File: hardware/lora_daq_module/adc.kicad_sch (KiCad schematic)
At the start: 0 parts

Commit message: added ADC input filter schematic
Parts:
- added C1: 47nF, symbol Device:C
- added C3: 0.1uF, symbol Device:C
- added D1, D2: D, symbol Device:D
- added J2: Conn_01x04, symbol Connector_Generic:Conn_01x04
- added R1: 1k, symbol Device:R
- added R3, R4: 10k, symbol Device:R
- added U1: ADS1115IDGS, Package_SO:TSSOP-10_3x3mm_P0.5mm, symbol Analog_ADC:ADS1115IDGS
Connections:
- new net: D1.2 (A), D2.2 (A), J2.1 (Pin_1), R1.2
- new net: C1.1, R1.1, U1.4 (AIN0)
- new net: J2.3 (Pin_3), U1.6 (AIN2)
- new net +3.3V: C3.1, D1.1 (K), R3.1, R4.1, U1.8 (VDD)
- new net GND: C1.2, C3.2, D2.1 (K), J2.2 (Pin_2), U1.1 (ADDR), U1.3 (GND), U1.5 (AIN1), U1.7 (AIN3)
- new net GPIO: U1.2 (ALERT/RDY)
- new net Input/5V: J2.4 (Pin_4)
- new net SCL: R3.2, U1.10 (SCL)
- new net SDA: R4.2, U1.9 (SDA)

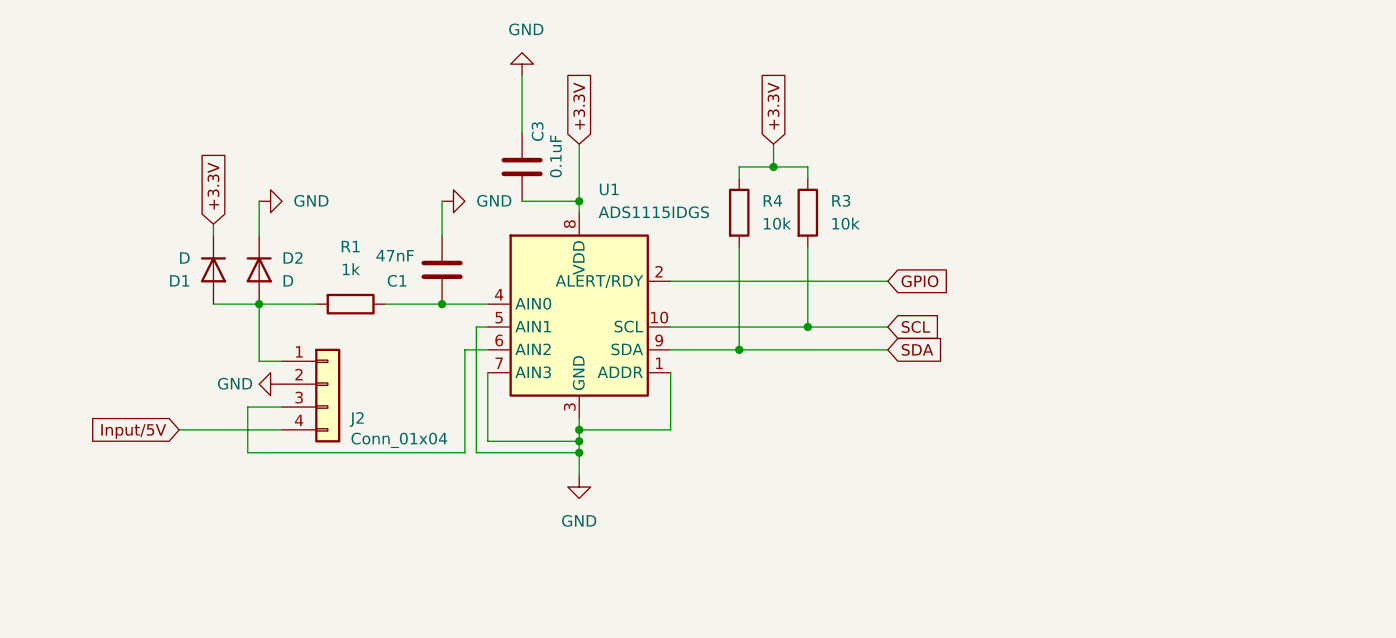
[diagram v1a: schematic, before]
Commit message: Updated the Adc circuit w/filters
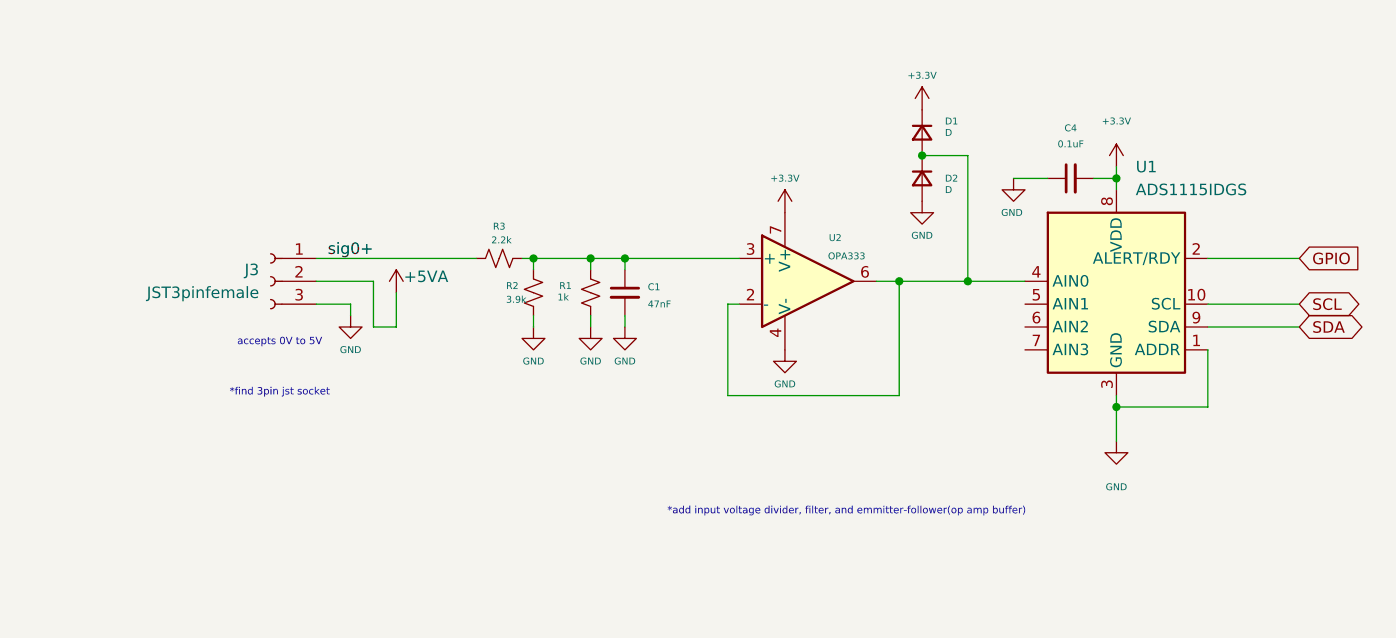
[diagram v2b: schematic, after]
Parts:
- removed C1: 47nF, symbol Device:C
- removed C3: 0.1uF, symbol Device:C
- removed D1, D2: D, symbol Device:D
- removed J2: Conn_01x04, symbol Connector_Generic:Conn_01x04
- removed R1: 1k, symbol Device:R
- removed R3, R4: 10k, symbol Device:R
- added C1: 47nF, symbol Device:C_Small
- added C4: 0.1uF, symbol Device:C_Small
- added D1, D2: D, symbol Device:D_Small
- added J3: JST3pinfemale, symbol Connector:Conn_01x03_Socket
- added R1: 1k, symbol Device:R_Small_US
- added R2: 3.9k, symbol Device:R_Small_US
- added R3: 2.2k, symbol Device:R_Small_US
- added U2: OPA333, Package_SO:SOIC-8_3.9x4.9mm_P1.27mm, symbol Amplifier_Operational:OPA333xxD
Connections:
- net +3.3V: now also C4.2, D1.1 (K), U2.7 (V+)
- net GND: now also C1.2, C4.1, D2.2 (A), J3.3 (Pin_3), R1.1, R2.2, U2.4 (V-); no longer U1.5 (AIN1), U1.7 (AIN3)
- net at U1.4 (AIN0): now also D1.2 (A), D2.1 (K), U2.2 (-), U2.6
- new net: C1.1, R1.2, R2.1, R3.2, U2.3 (+)
- new net +5VA: J3.2 (Pin_2)
- new net sig0+: J3.1 (Pin_1), R3.1
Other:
- note added: "*add input voltage divider, filter, and emmitter-follower(op amp buffer)"
- note added: "*find 3pin jst socket"
- note added: "accepts 0V to 5V"
- moved on the sheet: U1

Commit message: modified ADC input filter schematic
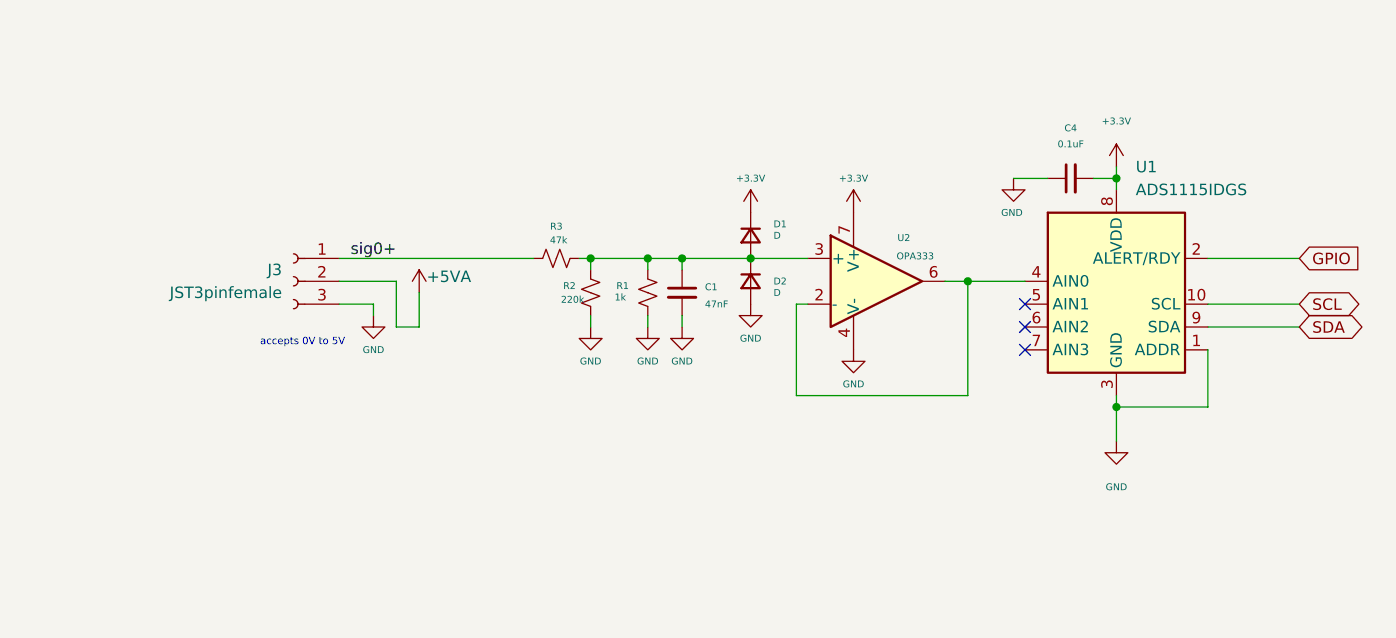
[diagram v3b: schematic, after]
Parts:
- R2: value 3.9k -> 220k
- R3: value 2.2k -> 47k
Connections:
- net at C1.1, R1.2, R2.1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: now also D1.2 (A), D2.1 (K)
- net at U1.4 (AIN0), U2.2 (-), U2.6: no longer D1.2 (A), D2.1 (K)
- no-connect marks 0 -> 3
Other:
- note removed: "*add input voltage divider, filter, and emmitter-follower(op amp buffer)"
- note removed: "*find 3pin jst socket"
- moved on the sheet: C1, D1, D2, J3, R1, R2, R3, U2

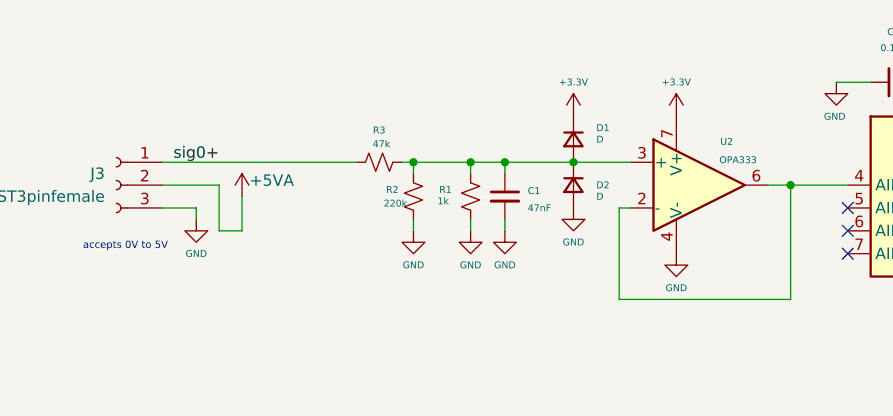
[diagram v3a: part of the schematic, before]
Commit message: adjusted ADC input filter power rails, added commets
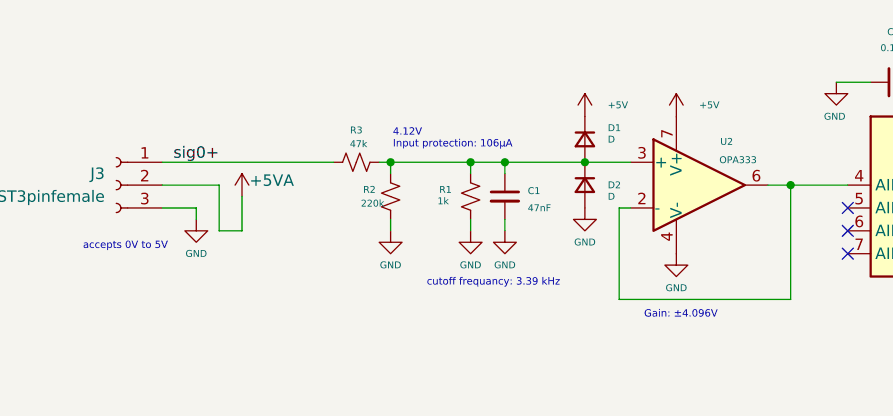
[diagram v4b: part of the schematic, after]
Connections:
- net +3.3V: no longer D1.1 (K), U2.7 (V+)
- new net +5V: D1.1 (K), U2.7 (V+)
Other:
- note added: "4.12V Input protection: 106µA"
- note added: "Gain: ±4.096V"
- note added: "cutoff frequancy: 3.39 kHz"
- moved on the sheet: D1, D2, R2, R3

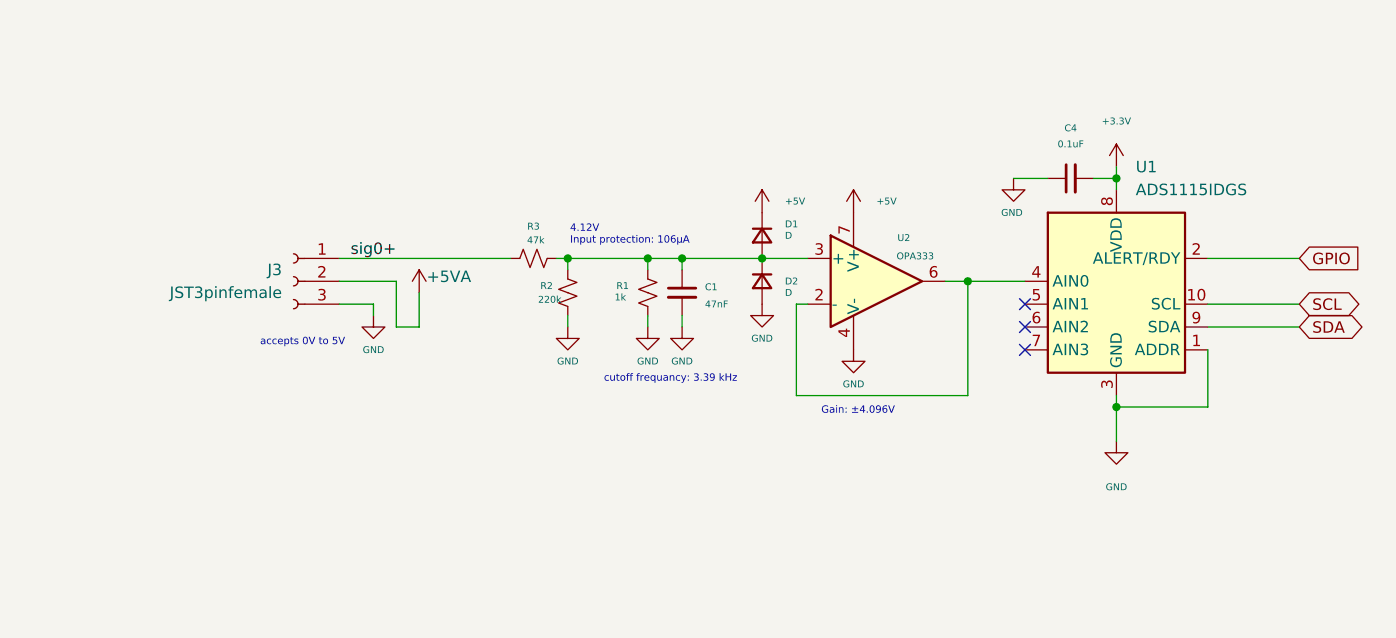
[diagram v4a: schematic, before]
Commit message: updated power schematic to include power switching IC for battery/usb power, minor changes to lora module schematic, added footprints to all component and began with the preliminary layout based on data sheet and application note reccomendations for each component.
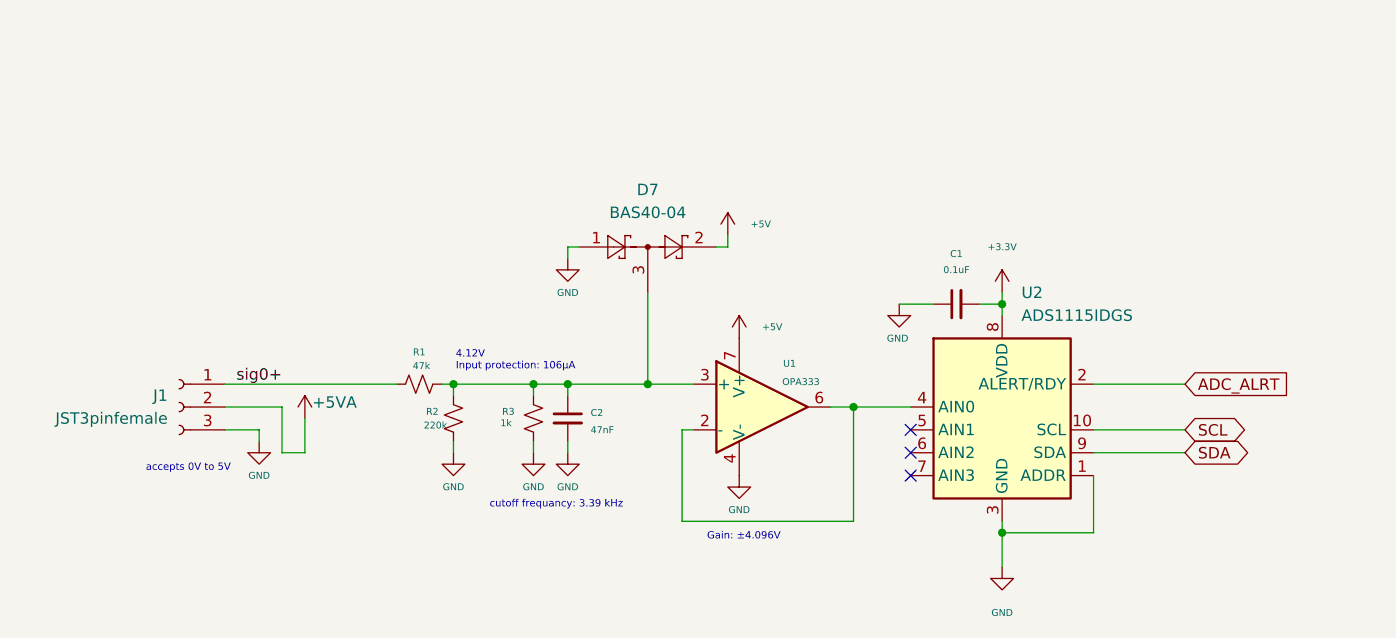
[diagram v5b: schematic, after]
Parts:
- removed D1, D2: D, symbol Device:D_Small
- added D7: BAS40-04, Package_TO_SOT_SMD:SOT-23, symbol Diode:BAS40-04
- C1: renamed from C4; footprint (none) -> Capacitor_SMD:C_0603_1608Metric
- C2: renamed from C1; footprint (none) -> Capacitor_SMD:C_0603_1608Metric
- J1: renamed from J3; footprint (none) -> Connector_JST:JST_EH_B3B-EH-A_1x03_P2.50mm_Vertical
- R1: renamed from R3; footprint (none) -> Resistor_SMD:R_0603_1608Metric
- R2: footprint (none) -> Resistor_SMD:R_0603_1608Metric
- R3: renamed from R1; footprint (none) -> Resistor_SMD:R_0603_1608Metric
- renumbered U2 to U1, U1 to U2
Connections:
- net +5V: now also D7.2
- net GND: now also D7.1
- net at C2.1, R1.2, R2.1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: now also D7.3
- net GPIO renamed ADC_ALRT
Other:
- moved on the sheet: C1, C2, J1, R1, R2, R3, U1, U2

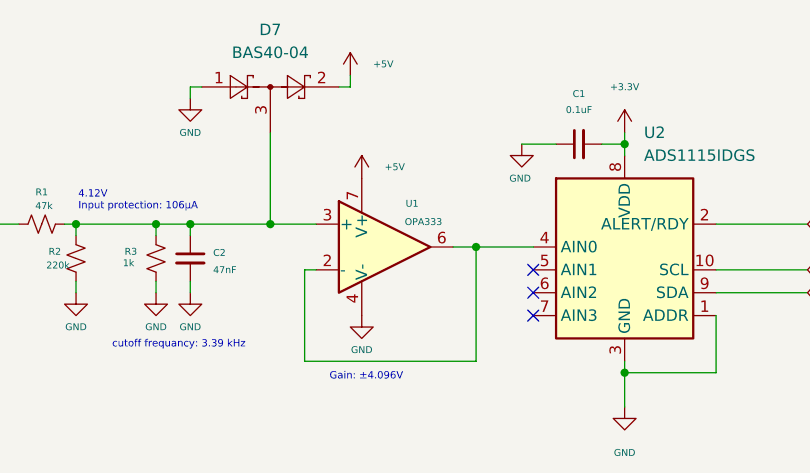
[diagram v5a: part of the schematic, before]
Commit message: setup BOM columns
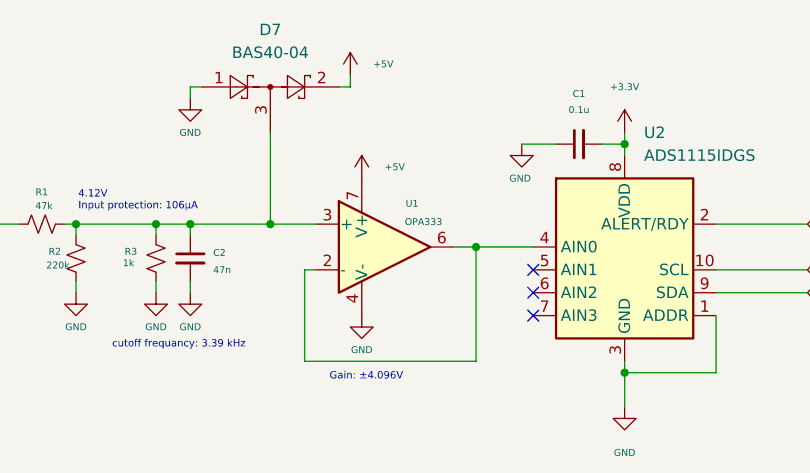
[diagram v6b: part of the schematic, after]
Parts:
- C1: value 0.1uF -> 0.1u
- C2: value 47nF -> 47n
